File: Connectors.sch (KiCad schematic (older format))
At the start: 4 parts

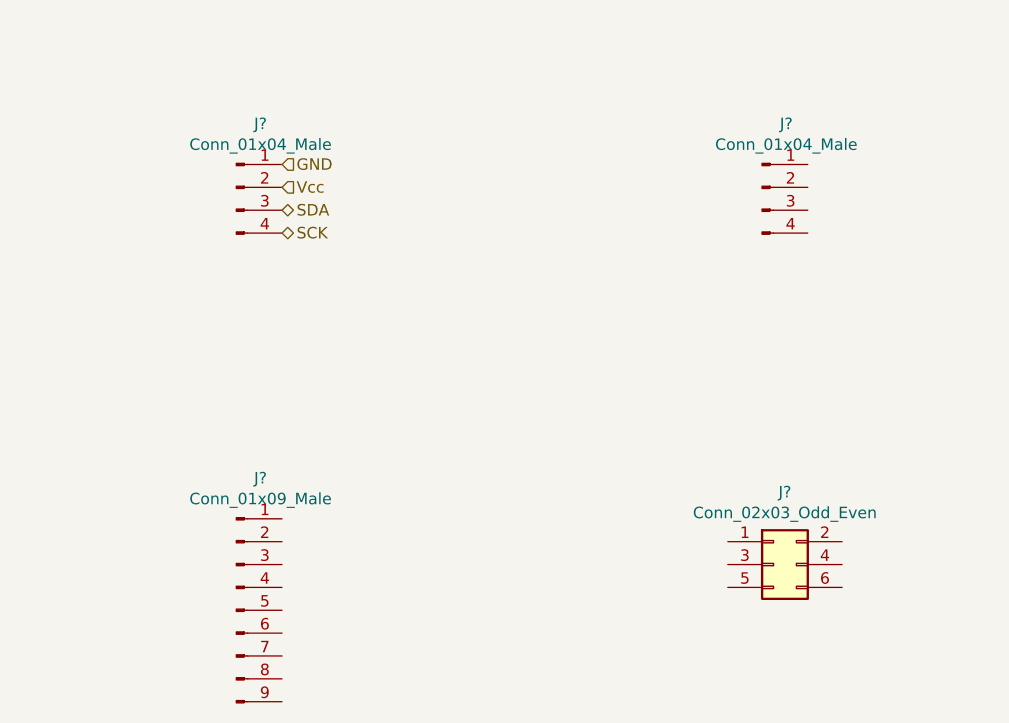
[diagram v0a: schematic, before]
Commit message: Annotated and edited symbol values.
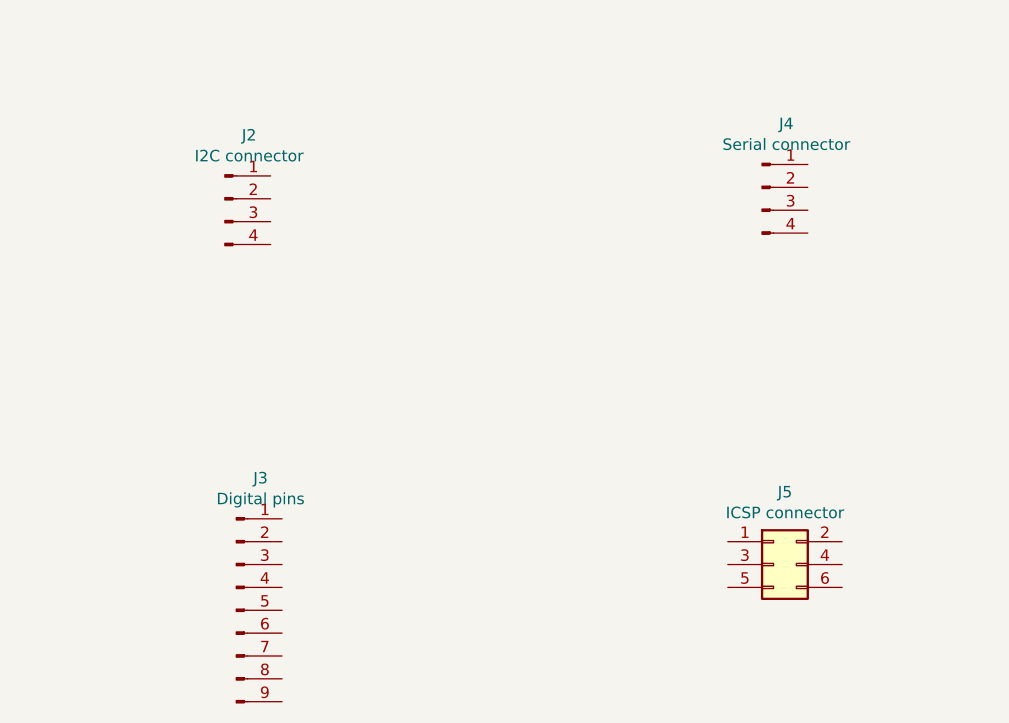
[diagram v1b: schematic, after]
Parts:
- removed J?: Conn_01x04_Male, symbol Connector:Conn_01x04_Male
- added J2: I2C connector, Connector_PinHeader_2.54mm:PinHeader_1x04_P2.54mm_Vertical, symbol Connector:Conn_01x04_Male
- J3: renamed from J?; value Conn_01x09_Male -> Digital pins; footprint (none) -> Connector_PinHeader_2.54mm:PinHeader_1x09_P2.54mm_Vertical
- J4: renamed from J?; value Conn_01x04_Male -> Serial connector; footprint (none) -> Connector_PinHeader_2.54mm:PinHeader_1x04_P2.54mm_Vertical
- J5: renamed from J?; value Conn_02x03_Odd_Even -> ICSP connector; footprint (none) -> Connector_PinHeader_2.54mm:PinHeader_2x03_P2.54mm_Vertical
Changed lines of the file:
@@
 $EndDescr
 $Comp
-L Connector:Conn_01x04_Male J?
-U 1 1 5B7FE24C
-P 4200 2700
-F 0 "J?" H 4306 2978 50  0000 C CNN
-F 1 "Conn_01x04_Male" H 4306 2887 50  0000 C CNN
-F 2 "" H 4200 2700 50  0001 C CNN
-F 3 "~" H 4200 2700 50  0001 C CNN
-	1    4200 2700
-	1    0    0    -1
-$EndComp
-Text HLabel 4400 2600 2    50   Input ~ 0
-GND
-Text HLabel 4400 2700 2    50   Input ~ 0
-Vcc
-Text HLabel 4400 2800 2    50   BiDi ~ 0
-SDA
-Text HLabel 4400 2900 2    50   BiDi ~ 0
-SCK
-$Comp
-L Connector:Conn_01x09_Male J?
+L Connector:Conn_01x09_Male J3
 U 1 1 5B7FEDEF
 P 4200 4550
-F 0 "J?" H 4306 5128 50  0000 C CNN
-F 1 "Conn_01x09_Male" H 4306 5037 50  0000 C CNN
-F 2 "" H 4200 4550 50  0001 C CNN
+F 0 "J3" H 4306 5128 50  0000 C CNN
+F 1 "Digital pins" H 4306 5037 50  0000 C CNN
+F 2 "Connector_PinHeader_2.54mm:PinHeader_1x09_P2.54mm_Vertical" H 4200 4550 50  0001 C CNN
 F 3 "~" H 4200 4550 50  0001 C CNN
 	1    4200 4550
@@
 $EndComp
 $Comp
-L Connector:Conn_01x04_Male J?
+L Connector:Conn_01x04_Male J4
 U 1 1 5B7FEE85
 P 6500 2700
-F 0 "J?" H 6606 2978 50  0000 C CNN
-F 1 "Conn_01x04_Male" H 6606 2887 50  0000 C CNN
-F 2 "" H 6500 2700 50  0001 C CNN
+F 0 "J4" H 6606 2978 50  0000 C CNN
+F 1 "Serial connector" H 6606 2887 50  0000 C CNN
+F 2 "Connector_PinHeader_2.54mm:PinHeader_1x04_P2.54mm_Vertical" H 6500 2700 50  0001 C CNN
 F 3 "~" H 6500 2700 50  0001 C CNN
 	1    6500 2700
@@
 $EndComp
 $Comp
-L Connector_Generic:Conn_02x03_Odd_Even J?
+L Connector_Generic:Conn_02x03_Odd_Even J5
 U 1 1 5B7FEF30
 P 6550 4350
-F 0 "J?" H 6600 4667 50  0000 C CNN
-F 1 "Conn_02x03_Odd_Even" H 6600 4576 50  0000 C CNN
-F 2 "" H 6550 4350 50  0001 C CNN
+F 0 "J5" H 6600 4667 50  0000 C CNN
+F 1 "ICSP connector" H 6600 4576 50  0000 C CNN
+F 2 "Connector_PinHeader_2.54mm:PinHeader_2x03_P2.54mm_Vertical" H 6550 4350 50  0001 C CNN
 F 3 "~" H 6550 4350 50  0001 C CNN
 	1    6550 4350
 	1    0    0    -1
 $EndComp
+$Comp
+L Connector:Conn_01x04_Male J2
+U 1 1 5B800CA7
+P 4150 2750
+F 0 "J2" H 4256 3028 50  0000 C CNN
+F 1 "I2C connector" H 4256 2937 50  0000 C CNN
+F 2 "Connector_PinHeader_2.54mm:PinHeader_1x04_P2.54mm_Vertical" H 4150 2750 50  0001 C CNN
+F 3 "~" H 4150 2750 50  0001 C CNN
+	1    4150 2750
+	1    0    0    -1
+$EndComp

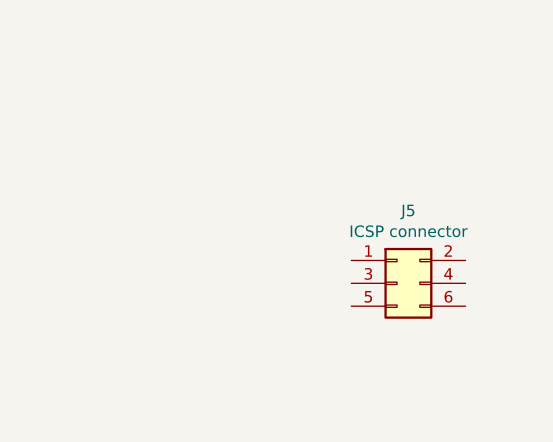
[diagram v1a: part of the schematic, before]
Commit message: Labeled the ICSP connector.
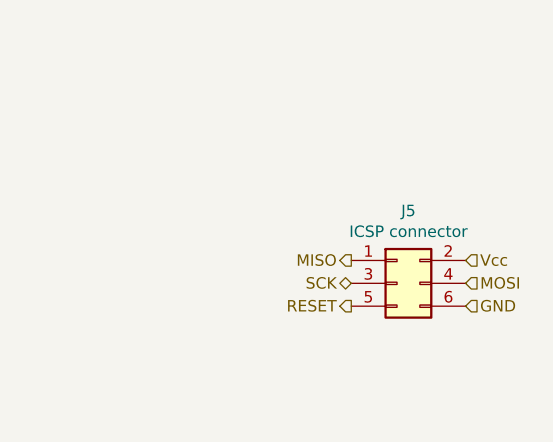
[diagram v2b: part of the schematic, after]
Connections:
- net MISO: now reaches J5.1 (Pin_1)
- net Vcc: now reaches J5.2 (Pin_2)
- net SCK: now reaches J5.3 (Pin_3)
- net MOSI: now reaches J5.4 (Pin_4)
- net RESET: now reaches J5.5 (Pin_5)
- net GND: now reaches J5.6 (Pin_6)
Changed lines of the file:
@@
 	1    0    0    -1
 $EndComp
+Text HLabel 6850 4250 2    50   Input ~ 0
+Vcc
+Text HLabel 6350 4250 0    50   Output ~ 0
+MISO
+Text HLabel 6350 4450 0    50   Output ~ 0
+RESET
+Text HLabel 6350 4350 0    50   BiDi ~ 0
+SCK
+Text HLabel 6850 4450 2    50   Input ~ 0
+GND
+Text HLabel 6850 4350 2    50   Input ~ 0
+MOSI
 $EndSCHEMATC

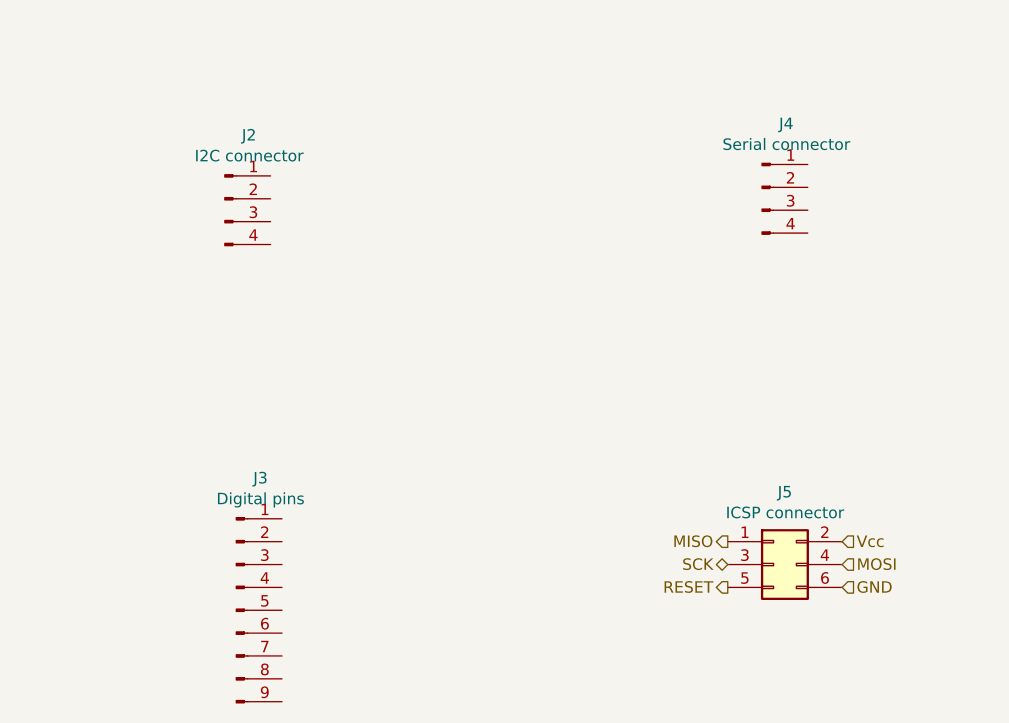
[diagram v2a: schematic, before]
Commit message: Wired MCU.
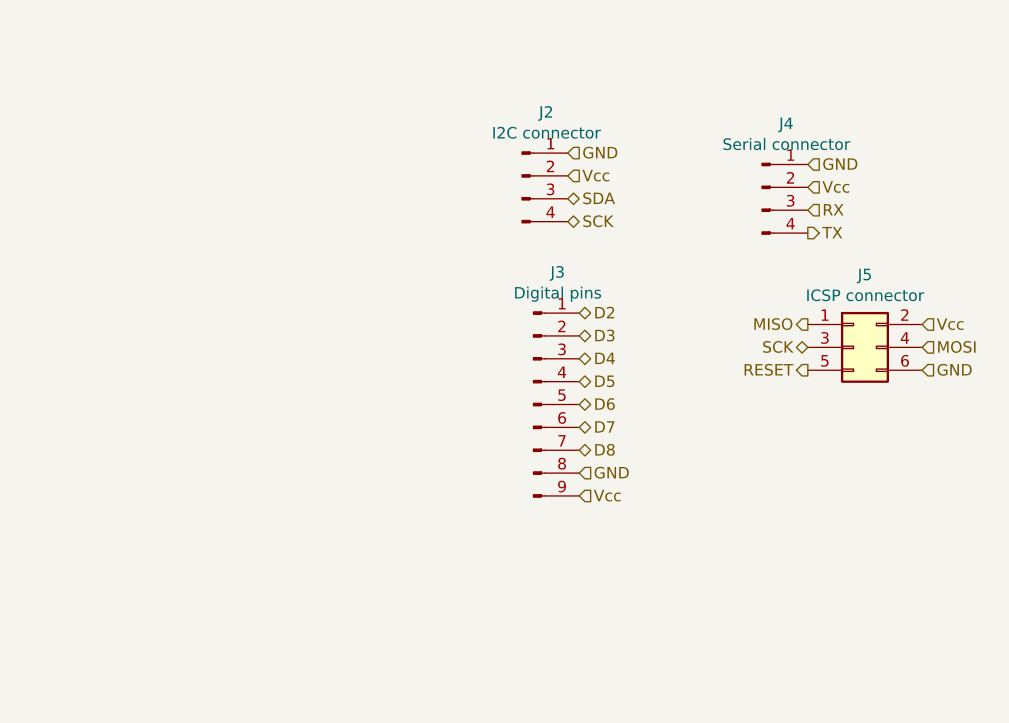
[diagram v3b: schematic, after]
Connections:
- net GND: now also J2.1 (Pin_1), J3.8 (Pin_8), J4.1 (Pin_1)
- net SCK: now also J2.4 (Pin_4)
- net Vcc: now also J2.2 (Pin_2), J3.9 (Pin_9), J4.2 (Pin_2)
- net D2: now reaches J3.1 (Pin_1)
- net D3: now reaches J3.2 (Pin_2)
- net D4: now reaches J3.3 (Pin_3)
- net D5: now reaches J3.4 (Pin_4)
- net D6: now reaches J3.5 (Pin_5)
- net D7: now reaches J3.6 (Pin_6)
- net D8: now reaches J3.7 (Pin_7)
- net RX: now reaches J4.3 (Pin_3)
- net TX: now reaches J4.4 (Pin_4)
- net SDA: now reaches J2.3 (Pin_3)
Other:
- moved on the sheet: J2, J3, J5
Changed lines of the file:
@@
 L Connector:Conn_01x09_Male J3
 U 1 1 5B7FEDEF
-P 4200 4550
-F 0 "J3" H 4306 5128 50  0000 C CNN
-F 1 "Digital pins" H 4306 5037 50  0000 C CNN
-F 2 "Connector_PinHeader_2.54mm:PinHeader_1x09_P2.54mm_Vertical" H 4200 4550 50  0001 C CNN
-F 3 "~" H 4200 4550 50  0001 C CNN
-	1    4200 4550
+P 5500 3650
+F 0 "J3" H 5606 4228 50  0000 C CNN
+F 1 "Digital pins" H 5606 4137 50  0000 C CNN
+F 2 "Connector_PinHeader_2.54mm:PinHeader_1x09_P2.54mm_Vertical" H 5500 3650 50  0001 C CNN
+F 3 "~" H 5500 3650 50  0001 C CNN
+	1    5500 3650
 	1    0    0    -1
 $EndComp
@@
 L Connector_Generic:Conn_02x03_Odd_Even J5
 U 1 1 5B7FEF30
-P 6550 4350
-F 0 "J5" H 6600 4667 50  0000 C CNN
-F 1 "ICSP connector" H 6600 4576 50  0000 C CNN
-F 2 "Connector_PinHeader_2.54mm:PinHeader_2x03_P2.54mm_Vertical" H 6550 4350 50  0001 C CNN
-F 3 "~" H 6550 4350 50  0001 C CNN
-	1    6550 4350
+P 6900 3400
+F 0 "J5" H 6950 3717 50  0000 C CNN
+F 1 "ICSP connector" H 6950 3626 50  0000 C CNN
+F 2 "Connector_PinHeader_2.54mm:PinHeader_2x03_P2.54mm_Vertical" H 6900 3400 50  0001 C CNN
+F 3 "~" H 6900 3400 50  0001 C CNN
+	1    6900 3400
 	1    0    0    -1
 $EndComp
@@
 L Connector:Conn_01x04_Male J2
 U 1 1 5B800CA7
-P 4150 2750
-F 0 "J2" H 4256 3028 50  0000 C CNN
-F 1 "I2C connector" H 4256 2937 50  0000 C CNN
-F 2 "Connector_PinHeader_2.54mm:PinHeader_1x04_P2.54mm_Vertical" H 4150 2750 50  0001 C CNN
-F 3 "~" H 4150 2750 50  0001 C CNN
-	1    4150 2750
+P 5450 2650
+F 0 "J2" H 5556 2928 50  0000 C CNN
+F 1 "I2C connector" H 5556 2837 50  0000 C CNN
+F 2 "Connector_PinHeader_2.54mm:PinHeader_1x04_P2.54mm_Vertical" H 5450 2650 50  0001 C CNN
+F 3 "~" H 5450 2650 50  0001 C CNN
+	1    5450 2650
 	1    0    0    -1
 $EndComp
-Text HLabel 6850 4250 2    50   Input ~ 0
+Text HLabel 7200 3300 2    50   Input ~ 0
 Vcc
-Text HLabel 6350 4250 0    50   Output ~ 0
+Text HLabel 6700 3300 0    50   Output ~ 0
 MISO
-Text HLabel 6350 4450 0    50   Output ~ 0
+Text HLabel 6700 3500 0    50   Output ~ 0
 RESET
-Text HLabel 6350 4350 0    50   BiDi ~ 0
+Text HLabel 6700 3400 0    50   BiDi ~ 0
 SCK
-Text HLabel 6850 4450 2    50   Input ~ 0
+Text HLabel 7200 3500 2    50   Input ~ 0
 GND
-Text HLabel 6850 4350 2    50   Input ~ 0
+Text HLabel 7200 3400 2    50   Input ~ 0
 MOSI
+Text HLabel 5700 3250 2    50   BiDi ~ 0
+D2
+Text HLabel 5700 3350 2    50   BiDi ~ 0
+D3
+Text HLabel 5700 3450 2    50   BiDi ~ 0
+D4
+Text HLabel 5700 3550 2    50   BiDi ~ 0
+D5
+Text HLabel 5700 3650 2    50   BiDi ~ 0
+D6
+Text HLabel 5700 3750 2    50   BiDi ~ 0
+D7
+Text HLabel 5700 3850 2    50   BiDi ~ 0
+D8
+Text HLabel 5700 3950 2    50   Input ~ 0
+GND
+Text HLabel 5700 4050 2    50   Input ~ 0
+Vcc
+Text HLabel 5650 2550 2    50   Input ~ 0
+GND
+Text HLabel 6700 2600 2    50   Input ~ 0
+GND
+Text HLabel 5650 2650 2    50   Input ~ 0
+Vcc
+Text HLabel 6700 2700 2    50   Input ~ 0
+Vcc
+Text HLabel 5650 2750 2    50   BiDi ~ 0
+SDA
+Text HLabel 5650 2850 2    50   BiDi ~ 0
+SCK
+Text HLabel 6700 2800 2    50   Input ~ 0
+RX
+Text HLabel 6700 2900 2    50   Output ~ 0
+TX
 $EndSCHEMATC

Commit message: Added informational graphics.
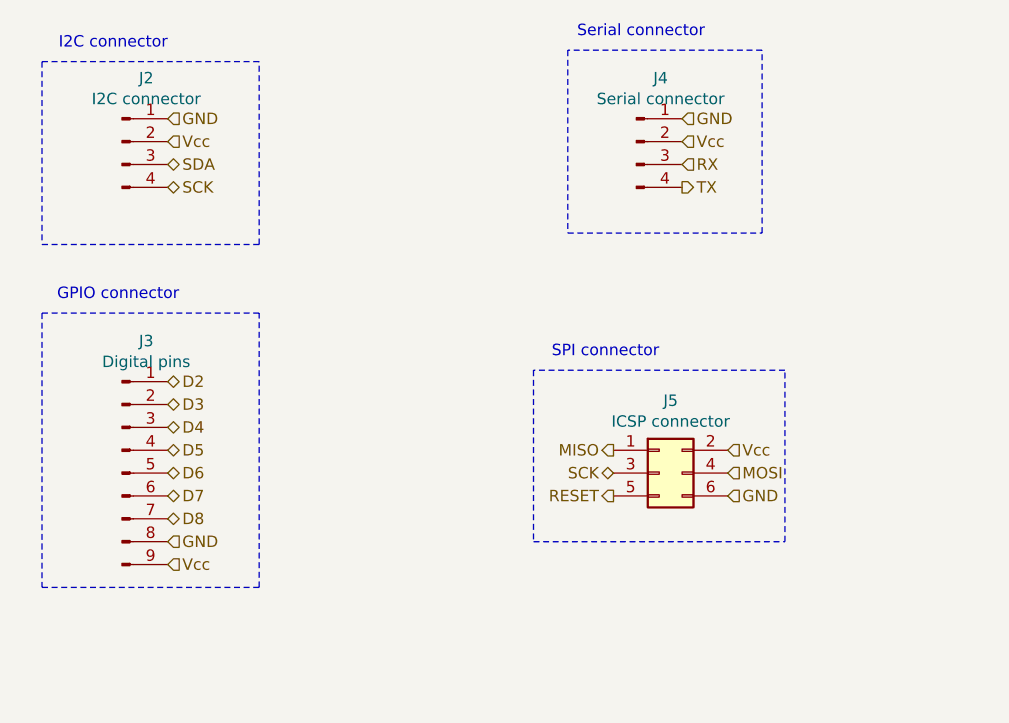
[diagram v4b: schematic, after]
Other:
- note added: "GPIO connector"
- note added: "I2C connector"
- note added: "SPI connector"
- note added: "Serial connector"
- moved on the sheet: J2, J3, J4, J5
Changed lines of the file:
@@
 L Connector:Conn_01x09_Male J3
 U 1 1 5B7FEDEF
-P 5500 3650
-F 0 "J3" H 5606 4228 50  0000 C CNN
-F 1 "Digital pins" H 5606 4137 50  0000 C CNN
-F 2 "Connector_PinHeader_2.54mm:PinHeader_1x09_P2.54mm_Vertical" H 5500 3650 50  0001 C CNN
-F 3 "~" H 5500 3650 50  0001 C CNN
-	1    5500 3650
+P 3700 3950
+F 0 "J3" H 3806 4528 50  0000 C CNN
+F 1 "Digital pins" H 3806 4437 50  0000 C CNN
+F 2 "Connector_PinHeader_2.54mm:PinHeader_1x09_P2.54mm_Vertical" H 3700 3950 50  0001 C CNN
+F 3 "~" H 3700 3950 50  0001 C CNN
+	1    3700 3950
 	1    0    0    -1
 $EndComp
@@
 L Connector:Conn_01x04_Male J4
 U 1 1 5B7FEE85
-P 6500 2700
-F 0 "J4" H 6606 2978 50  0000 C CNN
-F 1 "Serial connector" H 6606 2887 50  0000 C CNN
-F 2 "Connector_PinHeader_2.54mm:PinHeader_1x04_P2.54mm_Vertical" H 6500 2700 50  0001 C CNN
-F 3 "~" H 6500 2700 50  0001 C CNN
-	1    6500 2700
+P 5950 2500
+F 0 "J4" H 6056 2778 50  0000 C CNN
+F 1 "Serial connector" H 6056 2687 50  0000 C CNN
+F 2 "Connector_PinHeader_2.54mm:PinHeader_1x04_P2.54mm_Vertical" H 5950 2500 50  0001 C CNN
+F 3 "~" H 5950 2500 50  0001 C CNN
+	1    5950 2500
 	1    0    0    -1
 $EndComp
@@
 L Connector_Generic:Conn_02x03_Odd_Even J5
 U 1 1 5B7FEF30
-P 6900 3400
-F 0 "J5" H 6950 3717 50  0000 C CNN
-F 1 "ICSP connector" H 6950 3626 50  0000 C CNN
-F 2 "Connector_PinHeader_2.54mm:PinHeader_2x03_P2.54mm_Vertical" H 6900 3400 50  0001 C CNN
-F 3 "~" H 6900 3400 50  0001 C CNN
-	1    6900 3400
+P 6050 3950
+F 0 "J5" H 6100 4267 50  0000 C CNN
+F 1 "ICSP connector" H 6100 4176 50  0000 C CNN
+F 2 "Connector_PinHeader_2.54mm:PinHeader_2x03_P2.54mm_Vertical" H 6050 3950 50  0001 C CNN
+F 3 "~" H 6050 3950 50  0001 C CNN
+	1    6050 3950
 	1    0    0    -1
 $EndComp
@@
 L Connector:Conn_01x04_Male J2
 U 1 1 5B800CA7
-P 5450 2650
-F 0 "J2" H 5556 2928 50  0000 C CNN
-F 1 "I2C connector" H 5556 2837 50  0000 C CNN
-F 2 "Connector_PinHeader_2.54mm:PinHeader_1x04_P2.54mm_Vertical" H 5450 2650 50  0001 C CNN
-F 3 "~" H 5450 2650 50  0001 C CNN
-	1    5450 2650
+P 3700 2500
+F 0 "J2" H 3806 2778 50  0000 C CNN
+F 1 "I2C connector" H 3806 2687 50  0000 C CNN
+F 2 "Connector_PinHeader_2.54mm:PinHeader_1x04_P2.54mm_Vertical" H 3700 2500 50  0001 C CNN
+F 3 "~" H 3700 2500 50  0001 C CNN
+	1    3700 2500
 	1    0    0    -1
 $EndComp
-Text HLabel 7200 3300 2    50   Input ~ 0
+Text HLabel 6350 3850 2    50   Input ~ 0
 Vcc
-Text HLabel 6700 3300 0    50   Output ~ 0
+Text HLabel 5850 3850 0    50   Output ~ 0
 MISO
-Text HLabel 6700 3500 0    50   Output ~ 0
+Text HLabel 5850 4050 0    50   Output ~ 0
 RESET
-Text HLabel 6700 3400 0    50   BiDi ~ 0
+Text HLabel 5850 3950 0    50   BiDi ~ 0
 SCK
-Text HLabel 7200 3500 2    50   Input ~ 0
+Text HLabel 6350 4050 2    50   Input ~ 0
 GND
-Text HLabel 7200 3400 2    50   Input ~ 0
+Text HLabel 6350 3950 2    50   Input ~ 0
 MOSI
-Text HLabel 5700 3250 2    50   BiDi ~ 0
+Text HLabel 3900 3550 2    50   BiDi ~ 0
 D2
-Text HLabel 5700 3350 2    50   BiDi ~ 0
+Text HLabel 3900 3650 2    50   BiDi ~ 0
 D3
-Text HLabel 5700 3450 2    50   BiDi ~ 0
+Text HLabel 3900 3750 2    50   BiDi ~ 0
 D4
-Text HLabel 5700 3550 2    50   BiDi ~ 0
+Text HLabel 3900 3850 2    50   BiDi ~ 0
 D5
-Text HLabel 5700 3650 2    50   BiDi ~ 0
+Text HLabel 3900 3950 2    50   BiDi ~ 0
 D6
-Text HLabel 5700 3750 2    50   BiDi ~ 0
+Text HLabel 3900 4050 2    50   BiDi ~ 0
 D7
-Text HLabel 5700 3850 2    50   BiDi ~ 0
+Text HLabel 3900 4150 2    50   BiDi ~ 0
 D8
-Text HLabel 5700 3950 2    50   Input ~ 0
+Text HLabel 3900 4250 2    50   Input ~ 0
 GND
-Text HLabel 5700 4050 2    50   Input ~ 0
+Text HLabel 3900 4350 2    50   Input ~ 0
 Vcc
-Text HLabel 5650 2550 2    50   Input ~ 0
+Text HLabel 3900 2400 2    50   Input ~ 0
 GND
-Text HLabel 6700 2600 2    50   Input ~ 0
+Text HLabel 6150 2400 2    50   Input ~ 0
 GND
-Text HLabel 5650 2650 2    50   Input ~ 0
+Text HLabel 3900 2500 2    50   Input ~ 0
 Vcc
-Text HLabel 6700 2700 2    50   Input ~ 0
+Text HLabel 6150 2500 2    50   Input ~ 0
 Vcc
-Text HLabel 5650 2750 2    50   BiDi ~ 0
+Text HLabel 3900 2600 2    50   BiDi ~ 0
 SDA
-Text HLabel 5650 2850 2    50   BiDi ~ 0
+Text HLabel 3900 2700 2    50   BiDi ~ 0
 SCK
-Text HLabel 6700 2800 2    50   Input ~ 0
+Text HLabel 6150 2600 2    50   Input ~ 0
 RX
-Text HLabel 6700 2900 2    50   Output ~ 0
+Text HLabel 6150 2700 2    50   Output ~ 0
 TX
+Wire Notes Line
+	3350 2150 3350 2950
+Wire Notes Line
+	3350 2950 4300 2950
+Wire Notes Line
+	4300 2950 4300 2150
+Wire Notes Line
+	4300 2150 3350 2150
+Wire Notes Line
+	3350 3250 3350 4450
+Wire Notes Line
+	3350 4450 4300 4450
+Wire Notes Line
+	4300 4450 4300 3250
+Wire Notes Line
+	4300 3250 3350 3250
+Wire Notes Line
+	5650 2100 5650 2900
+Wire Notes Line
+	5650 2900 6500 2900
+Wire Notes Line
+	6500 2900 6500 2100
+Wire Notes Line
+	6500 2100 5650 2100
+Wire Notes Line
+	5500 3500 5500 4250
+Wire Notes Line
+	5500 4250 6600 4250
+Wire Notes Line
+	6600 4250 6600 3500
+Wire Notes Line
+	6600 3500 5500 3500
+Text Notes 3900 2100 2    50   ~ 0
+I2C connector
+Text Notes 6250 2050 2    50   ~ 0
+Serial connector
+Text Notes 3950 3200 2    50   ~ 0
+GPIO connector
+Text Notes 6050 3450 2    50   ~ 0
+SPI connector
 $EndSCHEMATC
